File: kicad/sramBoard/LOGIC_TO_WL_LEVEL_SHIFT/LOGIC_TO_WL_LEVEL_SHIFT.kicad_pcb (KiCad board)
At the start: 4 copper layers, 32 parts, among them Q1193 PMOS, Q1194 NMOS, Q1195 PMOS, Q1196 NMOS, Q1197 PMOS, Q1198 NMOS, Q1199 PMOS, Q1200 NMOS, Q1201 PMOS, Q1202 NMOS, Q1203 PMOS, Q1204 NMOS, Q1205 PMOS, Q1206 NMOS, Q1207 PMOS, Q1208 NMOS, Q1209 PMOS, Q1210 NMOS, Q1211 PMOS, Q1212 NMOS, Q1213 PMOS, Q1214 NMOS, Q1215 PMOS, Q1216 NMOS, Q1217 PMOS, Q1218 NMOS, Q1219 PMOS, Q1220 NMOS, Q1221 PMOS, Q1222 NMOS, Q1223 PMOS, Q1224 NMOS

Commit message: cdcdcdcdcdcdcdcdcdcdc
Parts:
- removed Q1193, Q1195, Q1197, Q1199, Q1201, Q1203, Q1205, Q1207, Q1209, Q1211, Q1213, Q1215, Q1217, Q1219, Q1221, Q1223: PMOS, Package_TO_SOT_SMD:SOT-23
- added R1: 10kR, Resistor_SMD:R_0603_1608Metric, F.Cu at (86.0, 51.5)
- added R10: 10kR, Resistor_SMD:R_0603_1608Metric, F.Cu at (86.0, 92.0)
- added R11: 10kR, Resistor_SMD:R_0603_1608Metric, F.Cu at (86.0, 96.5)
- added R12: 10kR, Resistor_SMD:R_0603_1608Metric, F.Cu at (86.0, 101.2)
- added R13: 10kR, Resistor_SMD:R_0603_1608Metric, F.Cu at (86.0, 105.8)
- added R14: 10kR, Resistor_SMD:R_0603_1608Metric, F.Cu at (86.0, 110.2)
- added R15: 10kR, Resistor_SMD:R_0603_1608Metric, F.Cu at (86.0, 114.8)
- added R16: 10kR, Resistor_SMD:R_0603_1608Metric, F.Cu at (86.0, 119.2)
- added R2: 10kR, Resistor_SMD:R_0603_1608Metric, F.Cu at (86.0, 56.0)
- added R3: 10kR, Resistor_SMD:R_0603_1608Metric, F.Cu at (86.0, 60.5)
- added R4: 10kR, Resistor_SMD:R_0603_1608Metric, F.Cu at (86.0, 65.0)
- added R5: 10kR, Resistor_SMD:R_0603_1608Metric, F.Cu at (86.0, 69.5)
- added R6: 10kR, Resistor_SMD:R_0603_1608Metric, F.Cu at (86.0, 74.0)
- added R7: 10kR, Resistor_SMD:R_0603_1608Metric, F.Cu at (86.0, 78.8)
- added R8: 10kR, Resistor_SMD:R_0603_1608Metric, F.Cu at (86.0, 83.0)
- added R9: 10kR, Resistor_SMD:R_0603_1608Metric, F.Cu at (86.0, 87.5)
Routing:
- net /A_{11}: track 4.28 -> 0.00 mm
- net /A_{8}: track 4.26 -> 0.00 mm
- net /A_{10}: track 4.26 -> 0.00 mm
- net /A_{12}: track 4.23 -> 0.00 mm
- net /A_{0}: track 4.22 -> 0.00 mm
- net /A_{7}: track 4.20 -> 0.00 mm
- net /A_{4}: track 4.20 -> 0.00 mm
- net /A_{2}: track 4.20 -> 0.00 mm
- net /A_{1}: track 4.20 -> 0.00 mm
- net /A_{15}: track 4.20 -> 0.00 mm
- net /A_{13}: track 4.20 -> 0.00 mm
- net /A_{6}: track 4.18 -> 0.00 mm
- net /A_{3}: track 4.18 -> 0.00 mm
- net /A_{5}: track 4.13 -> 0.00 mm
- net /A_{14}: track 4.13 -> 0.00 mm
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
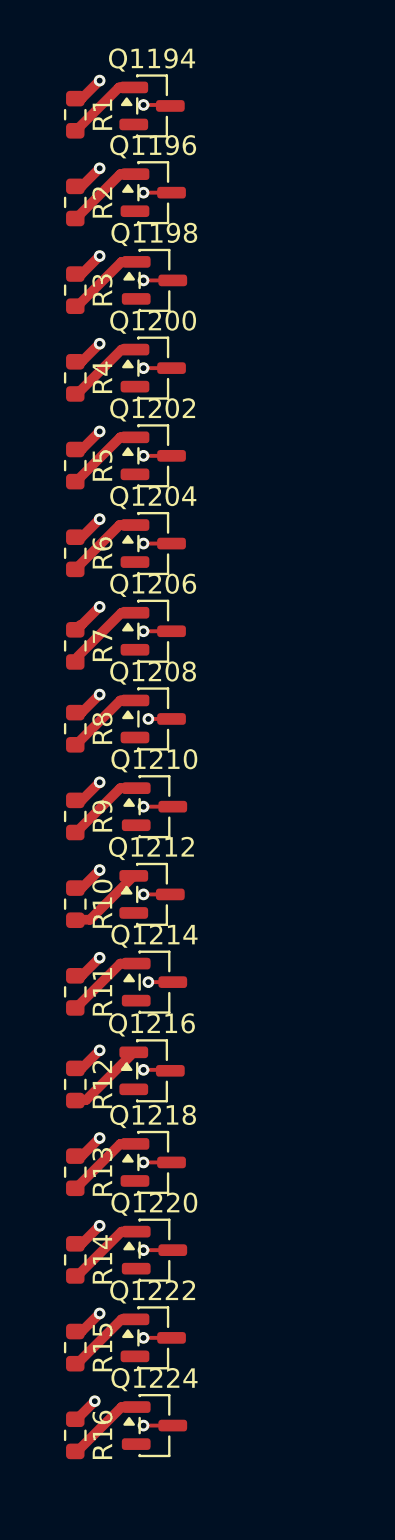
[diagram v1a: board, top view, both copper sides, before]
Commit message: fix main ram board
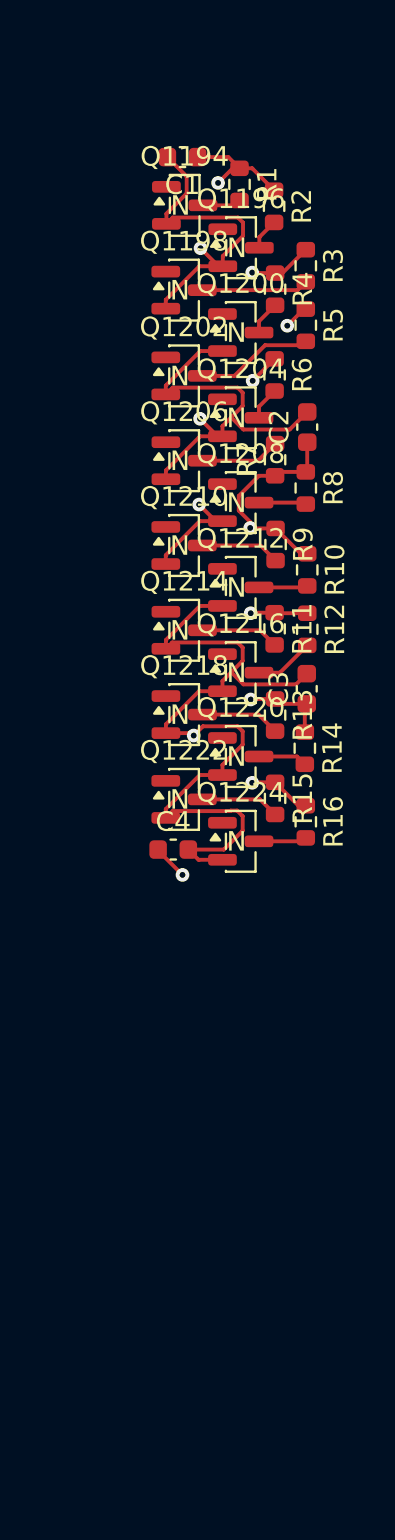
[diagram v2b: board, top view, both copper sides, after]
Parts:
- added C1: 100nC, Capacitor_SMD:C_0603_1608Metric, F.Cu at (91.5, 53.7)
- added C2: 100nC, Capacitor_SMD:C_0603_1608Metric, F.Cu at (97.9, 67.5)
- added C3: 100nC, Capacitor_SMD:C_0603_1608Metric, F.Cu at (97.9, 81.0)
- added C4: 100nC, Capacitor_SMD:C_0603_1608Metric, F.Cu at (91.0, 89.2)
- Q1194, Q1196, Q1198, Q1200, Q1202, Q1204, Q1206, Q1208, Q1210, Q1212, Q1214, Q1216, Q1218, Q1220, Q1222, Q1224: value NMOS -> Q_NMOS_GSD; footprint Package_TO_SOT_SMD:SOT-23 -> easyeda2kicad:SOT-23-N
- moved R16 33.6 mm to (97.8, 87.8)
- moved Q1224 30.3 mm to (94.6, 88.8)
- moved R15 30.0 mm to (96.2, 86.6)
- moved R14 28.8 mm to (97.8, 84.0)
- moved Q1222 27.7 mm to (91.7, 86.6)
- moved R12 26.2 mm to (97.9, 77.9)
- moved Q1220 25.7 mm to (94.6, 84.4)
- moved R13 25.6 mm to (96.2, 82.3)
- moved Q1218 23.0 mm to (91.7, 82.3)
- moved R11 21.2 mm to (96.2, 77.9)
- moved Q1216 20.9 mm to (94.6, 80.1)
- moved R10 20.9 mm to (97.9, 74.8)
- moved Q1214 18.1 mm to (91.7, 78.0)
- moved R9 17.3 mm to (96.3, 73.5)
- moved R8 17.1 mm to (97.8, 70.7)
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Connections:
- Q1194 pad 1: /~{Y_{0}} -> /A_{0}
- Q1194 pad 2: /A_{0} -> GND
- Q1194 pad 3: GND -> /~{Y_{0}}
- Q1196 pad 1: /~{Y_{1}} -> /A_{1}
- Q1196 pad 2: /A_{1} -> GND
- Q1196 pad 3: GND -> /~{Y_{1}}
- Q1198 pad 1: /~{Y_{2}} -> /A_{2}
- Q1198 pad 2: /A_{2} -> GND
- Q1198 pad 3: GND -> /~{Y_{2}}
- Q1200 pad 1: /~{Y_{3}} -> /A_{3}
- Q1200 pad 2: /A_{3} -> GND
- Q1200 pad 3: GND -> /~{Y_{3}}
- Q1202 pad 1: /~{Y_{4}} -> /A_{4}
- Q1202 pad 2: /A_{4} -> GND
- Q1202 pad 3: GND -> /~{Y_{4}}
- Q1204 pad 1: /~{Y_{5}} -> /A_{5}
- Q1204 pad 2: /A_{5} -> GND
- Q1204 pad 3: GND -> /~{Y_{5}}
- Q1206 pad 1: /~{Y_{6}} -> /A_{6}
- Q1206 pad 2: /A_{6} -> GND
- Q1206 pad 3: GND -> /~{Y_{6}}
- Q1208 pad 1: /~{Y_{7}} -> /A_{7}
- Q1208 pad 2: /A_{7} -> GND
- Q1208 pad 3: GND -> /~{Y_{7}}
- Q1210 pad 1: /~{Y_{8}} -> /A_{8}
- Q1210 pad 2: /A_{8} -> GND
- Q1210 pad 3: GND -> /~{Y_{8}}
- Q1212 pad 1: /~{Y_{9}} -> /A_{9}
- Q1212 pad 2: /A_{9} -> GND
- Q1212 pad 3: GND -> /~{Y_{9}}
- Q1214 pad 1: /~{Y_{10}} -> /A_{10}
- Q1214 pad 2: /A_{10} -> GND
- Q1214 pad 3: GND -> /~{Y_{10}}
- Q1216 pad 1: /~{Y_{11}} -> /A_{11}
- Q1216 pad 2: /A_{11} -> GND
- Q1216 pad 3: GND -> /~{Y_{11}}
- Q1218 pad 1: /~{Y_{12}} -> /A_{12}
- Q1218 pad 2: /A_{12} -> GND
- Q1218 pad 3: GND -> /~{Y_{12}}
- Q1220 pad 1: /~{Y_{13}} -> /A_{13}
- Q1220 pad 2: /A_{13} -> GND
- Q1220 pad 3: GND -> /~{Y_{13}}
- Q1222 pad 1: /~{Y_{14}} -> /A_{14}
- Q1222 pad 2: /A_{14} -> GND
- Q1222 pad 3: GND -> /~{Y_{14}}
- Q1224 pad 1: /~{Y_{15}} -> /A_{15}
- Q1224 pad 2: /A_{15} -> GND
- Q1224 pad 3: GND -> /~{Y_{15}}
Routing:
- net GND: track 24.0 -> 84.0 mm, vias 16 -> 4
- net +10V: track 22.1 -> 35.7 mm, vias 16 -> 9
- net /~{Y_{1}}: track 3.93 -> 1.61 mm
- net /~{Y_{5}}: track 4.00 -> 1.71 mm
- net /~{Y_{3}}: track 3.87 -> 1.74 mm
- net /~{Y_{4}}: track 3.93 -> 6.04 mm
- net /~{Y_{0}}: track 3.93 -> 1.98 mm
- net /~{Y_{2}}: track 3.93 -> 5.48 mm
- net /~{Y_{7}}: track 3.93 -> 2.43 mm
- net /~{Y_{15}}: track 3.93 -> 2.47 mm
- net /~{Y_{13}}: track 3.93 -> 2.52 mm
- net /~{Y_{9}}: track 3.81 -> 2.51 mm
- net /~{Y_{11}}: track 4.01 -> 3.05 mm
